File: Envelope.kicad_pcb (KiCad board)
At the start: 2 copper layers, 39.5 x 100 mm, 81 parts, among them J1 Conn_02x05_Odd_Even, J2 Conn_02x03_Odd_Even, J3 Conn_01x06, SW1 SW_SPDT_MSM, SW2 SW_SPDT_MSM, SW3 SW_Push, U1 TL072, U2 ATmega328PB-AU, U3 L7805, Y1 20MHz

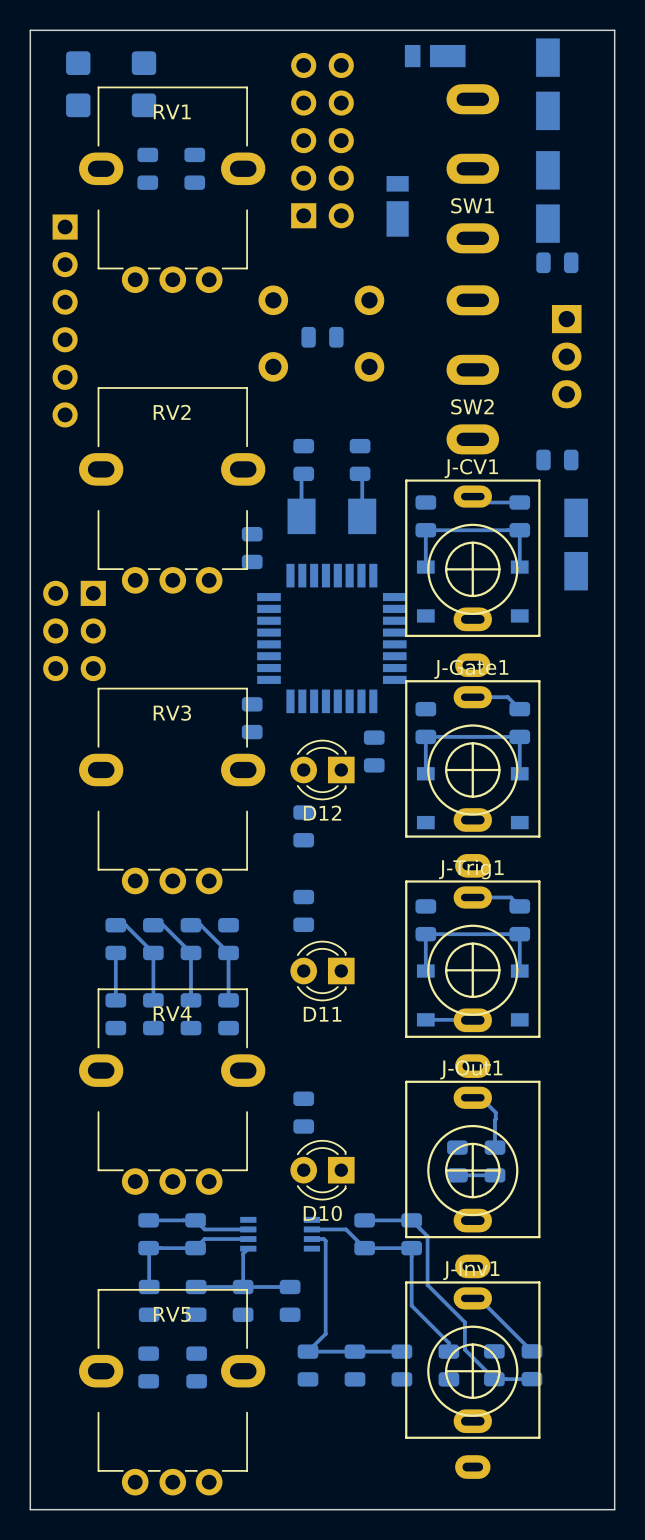
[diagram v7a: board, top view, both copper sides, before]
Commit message: Routed most signals.
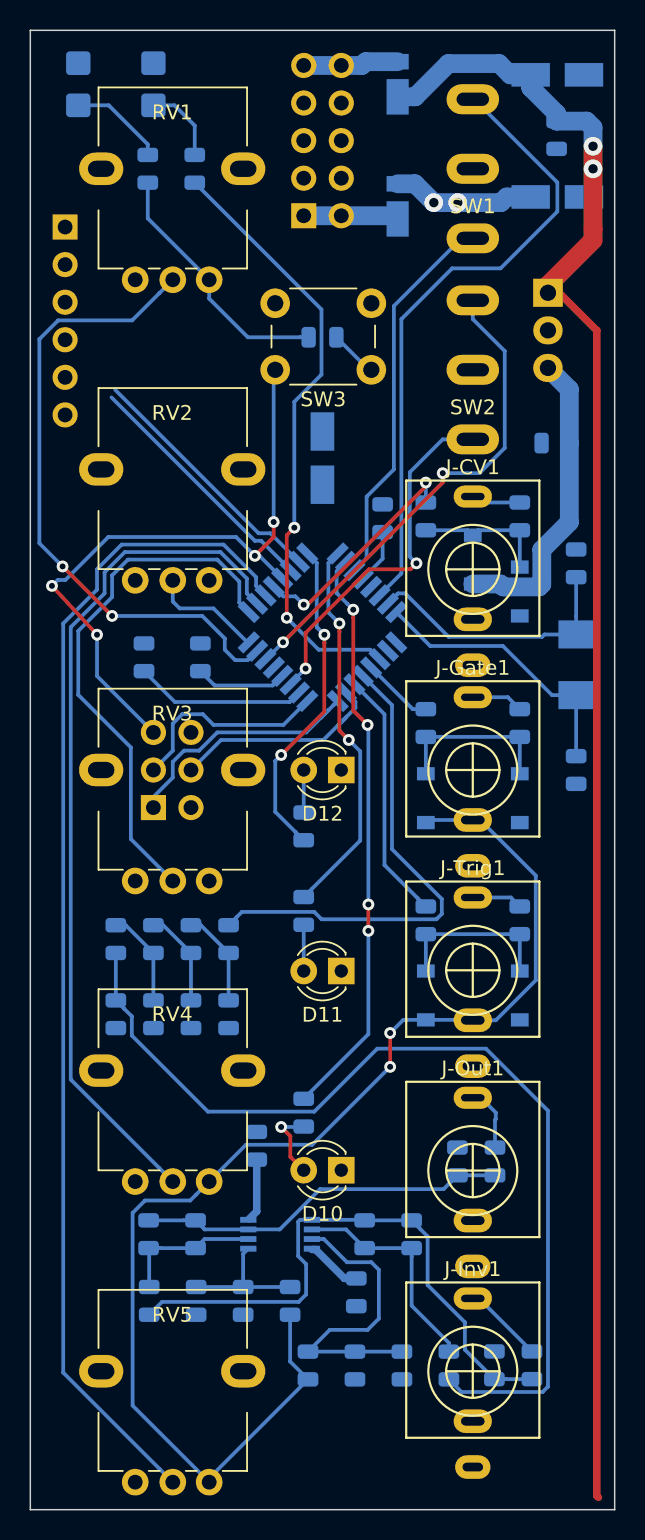
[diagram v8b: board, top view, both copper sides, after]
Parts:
- SW3: moved to F.Cu
- moved C20 25.5 mm to (144.4, 98.0), turned to 90 degrees
- moved C19 19.7 mm to (144.4, 84.1)
- moved Y1 19.3 mm to (144.4, 90.9), turned to 270 degrees
- moved C15 18.1 mm to (127.3, 77.0)
- moved C9 16.7 mm to (122.8, 123.4), turned to 90 degrees
- moved C17 15.8 mm to (131.3, 81.0), turned to 90 degrees
- moved J2 15.0 mm to (115.8, 100.6), turned to 0 degrees
- moved C10 11.9 mm to (129.5, 133.3)
- moved C18 10.4 mm to (115.2, 90.4)
- moved C13 8.64 mm to (143.1, 55.1), turned to 270 degrees
- moved C16 5.41 mm to (119.0, 90.4), turned to 270 degrees
- moved SW3 4.70 mm to (130.6, 71.0)
- moved D5 3.84 mm to (137.4, 83.8)
- moved D7 3.17 mm to (132.3, 51.7), turned to 90 degrees
- moved U3 2.18 mm to (142.5, 65.8)
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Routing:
- net +5V: track 3.19 -> 139.7 mm, vias 0 -> 2
- net +12V: track 0.00 -> 116.7 mm, vias 0 -> 2
- net /MCU328/PC4: track 0.00 -> 79.6 mm
- net Net-(C4-Pad1): track 3.20 -> 65.6 mm
- net /MCU328/PC3: track 0.00 -> 57.9 mm
- net Net-(J2-Pad5): track 0.00 -> 47.2 mm, vias 0 -> 4
- net /MCU328/PC0: track 0.00 -> 43.2 mm, vias 0 -> 2
- net /MCU328/PE1: track 0.00 -> 42.9 mm
- net /MCU328/PD7: track 0.00 -> 41.4 mm, vias 0 -> 2
- net /MCU328/PD4: track 0.00 -> 39.3 mm, vias 0 -> 4
- net /MCU328/PC2: track 0.00 -> 36.2 mm
- net /MCU328/PB1: track 0.00 -> 33.4 mm
- net /MCU328/PE3: track 0.00 -> 33.3 mm, vias 0 -> 2
- net /MCU328/PE0: track 0.00 -> 26.2 mm
- net /MCU328/PD3: track 0.00 -> 25.6 mm, vias 0 -> 2
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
